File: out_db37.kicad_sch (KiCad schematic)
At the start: 1 part, among them J1 DB37_Female

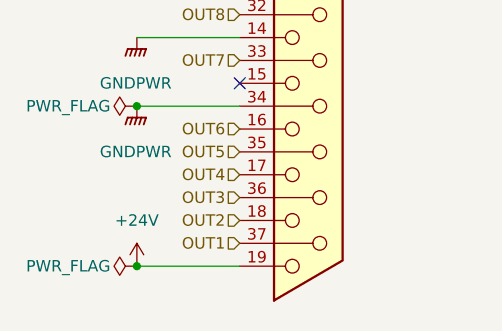
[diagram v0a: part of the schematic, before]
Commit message: Common power stage for field IO
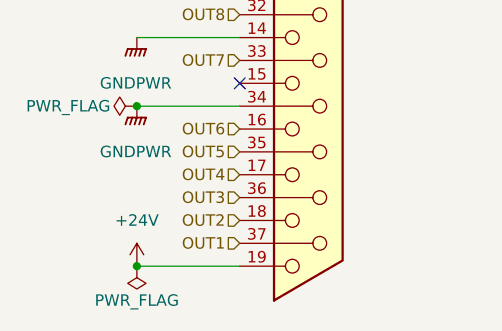
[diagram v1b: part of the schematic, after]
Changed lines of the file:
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@@
     (effects (font (size 1.27 1.27)) (justify right))
-  )
-  (symbol (lib_id "power:+24V") (at 189.23 46.99 0) (unit 1)
-    (in_bom yes) (on_board yes) (fields_autoplaced)
-    (property "Reference" "#PWR021" (id 0) (at 189.23 50.8 0)
-      (effects (font (size 1.27 1.27)) hide)
-    )
-    (property "Value" "+24V" (id 1) (at 189.23 41.91 0))
-    (property "Footprint" "" (id 2) (at 189.23 46.99 0)
-      (effects (font (size 1.27 1.27)) hide)
-    )
-    (property "Datasheet" "" (id 3) (at 189.23 46.99 0)
-      (effects (font (size 1.27 1.27)) hide)
-    )
-    (pin "1")
   )
   (symbol (lib_id "power:GNDPWR") (at 189.23 107.95 0) (unit 1)
     (in_bom yes) (on_board yes) (fields_autoplaced)
-    (property "Reference" "#PWR024" (id 0) (at 189.23 113.03 0)
+    (property "Reference" "#PWR027" (id 0) (at 189.23 113.03 0)
       (effects (font (size 1.27 1.27)) hide)
     )
@@
   (symbol (lib_id "power:+24V") (at 189.23 133.35 0) (unit 1)
     (in_bom yes) (on_board yes) (fields_autoplaced)
-    (property "Reference" "#PWR026" (id 0) (at 189.23 137.16 0)
+    (property "Reference" "#PWR029" (id 0) (at 189.23 137.16 0)
       (effects (font (size 1.27 1.27)) hide)
     )
@@
   (symbol (lib_id "power:GNDPWR") (at 189.23 115.57 0) (unit 1)
     (in_bom yes) (on_board yes) (fields_autoplaced)
-    (property "Reference" "#PWR025" (id 0) (at 189.23 120.65 0)
+    (property "Reference" "#PWR028" (id 0) (at 189.23 120.65 0)
       (effects (font (size 1.27 1.27)) hide)
     )
@@
     (pin "1")
   )
-  (symbol (lib_id "power:PWR_FLAG") (at 189.23 133.35 90) (unit 1)
+  (symbol (lib_id "power:PWR_FLAG") (at 189.23 133.35 180) (unit 1)
     (in_bom yes) (on_board yes)
-    (property "Reference" "#FLG0101" (id 0) (at 187.325 133.35 0)
+    (property "Reference" "#FLG02" (id 0) (at 189.23 135.255 0)
       (effects (font (size 1.27 1.27)) hide)
     )
-    (property "Value" "PWR_FLAG" (id 1) (at 181.61 133.35 90))
+    (property "Value" "PWR_FLAG" (id 1) (at 189.23 137.16 0))
     (property "Footprint" "" (id 2) (at 189.23 133.35 0)
       (effects (font (size 1.27 1.27)) hide)
@@
     (pin "1")
   )
+  (symbol (lib_id "power:+24V") (at 189.23 46.99 0) (unit 1)
+    (in_bom yes) (on_board yes) (fields_autoplaced)
+    (property "Reference" "#PWR024" (id 0) (at 189.23 50.8 0)
+      (effects (font (size 1.27 1.27)) hide)
+    )
+    (property "Value" "+24V" (id 1) (at 189.23 41.91 0))
+    (property "Footprint" "" (id 2) (at 189.23 46.99 0)
+      (effects (font (size 1.27 1.27)) hide)
+    )
+    (property "Datasheet" "" (id 3) (at 189.23 46.99 0)
+      (effects (font (size 1.27 1.27)) hide)
+    )
+    (pin "1")
+  )
   (symbol (lib_id "power:GNDPWR") (at 189.23 52.07 0) (unit 1)
     (in_bom yes) (on_board yes) (fields_autoplaced)
-    (property "Reference" "#PWR022" (id 0) (at 189.23 57.15 0)
+    (property "Reference" "#PWR025" (id 0) (at 189.23 57.15 0)
       (effects (font (size 1.27 1.27)) hide)
     )
@@
   (symbol (lib_id "power:PWR_FLAG") (at 189.23 115.57 90) (unit 1)
     (in_bom yes) (on_board yes)
-    (property "Reference" "#FLG0104" (id 0) (at 187.325 115.57 0)
+    (property "Reference" "#FLG01" (id 0) (at 187.325 115.57 0)
       (effects (font (size 1.27 1.27)) hide)
     )
@@
   (symbol (lib_id "power:GNDPWR") (at 189.23 82.55 0) (unit 1)
     (in_bom yes) (on_board yes) (fields_autoplaced)
-    (property "Reference" "#PWR023" (id 0) (at 189.23 87.63 0)
+    (property "Reference" "#PWR026" (id 0) (at 189.23 87.63 0)
       (effects (font (size 1.27 1.27)) hide)
     )
